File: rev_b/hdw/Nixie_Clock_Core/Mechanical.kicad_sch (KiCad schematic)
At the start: 40 parts

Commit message: lots of rev B control board schematic progress
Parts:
- renumbered H3101 to H?, H3104 to H?, H3106 to H?, H3102 to H?, H3103 to H?, H3107 to H?, H3105 to H?, H3108 to H?, MK3101 to MK?, MK3118 to MK?, MK3107 to MK?, MK3122 to MK?, MK3126 to MK?, MK3113 to MK?, MK3125 to MK?, MK3119 to MK?, MK3108 to MK?, MK3128 to MK?, MK3109 to MK?, MK3117 to MK?, MK3114 to MK?, MK3110 to MK?, MK3111 to MK?, MK3130 to MK?, MK3123 to MK?, MK3104 to MK?, MK3112 to MK?, MK3129 to MK?, MK3116 to MK?, MK3124 to MK?, MK3127 to MK?, MK3121 to MK?, MK3106 to MK?, MK3102 to MK?, MK3132 to MK?, MK3131 to MK?, MK3120 to MK?, MK3105 to MK?, MK3115 to MK?, MK3103 to MK?
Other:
- note added: "ENSURE STACK IS CORRECT HEIGHT"

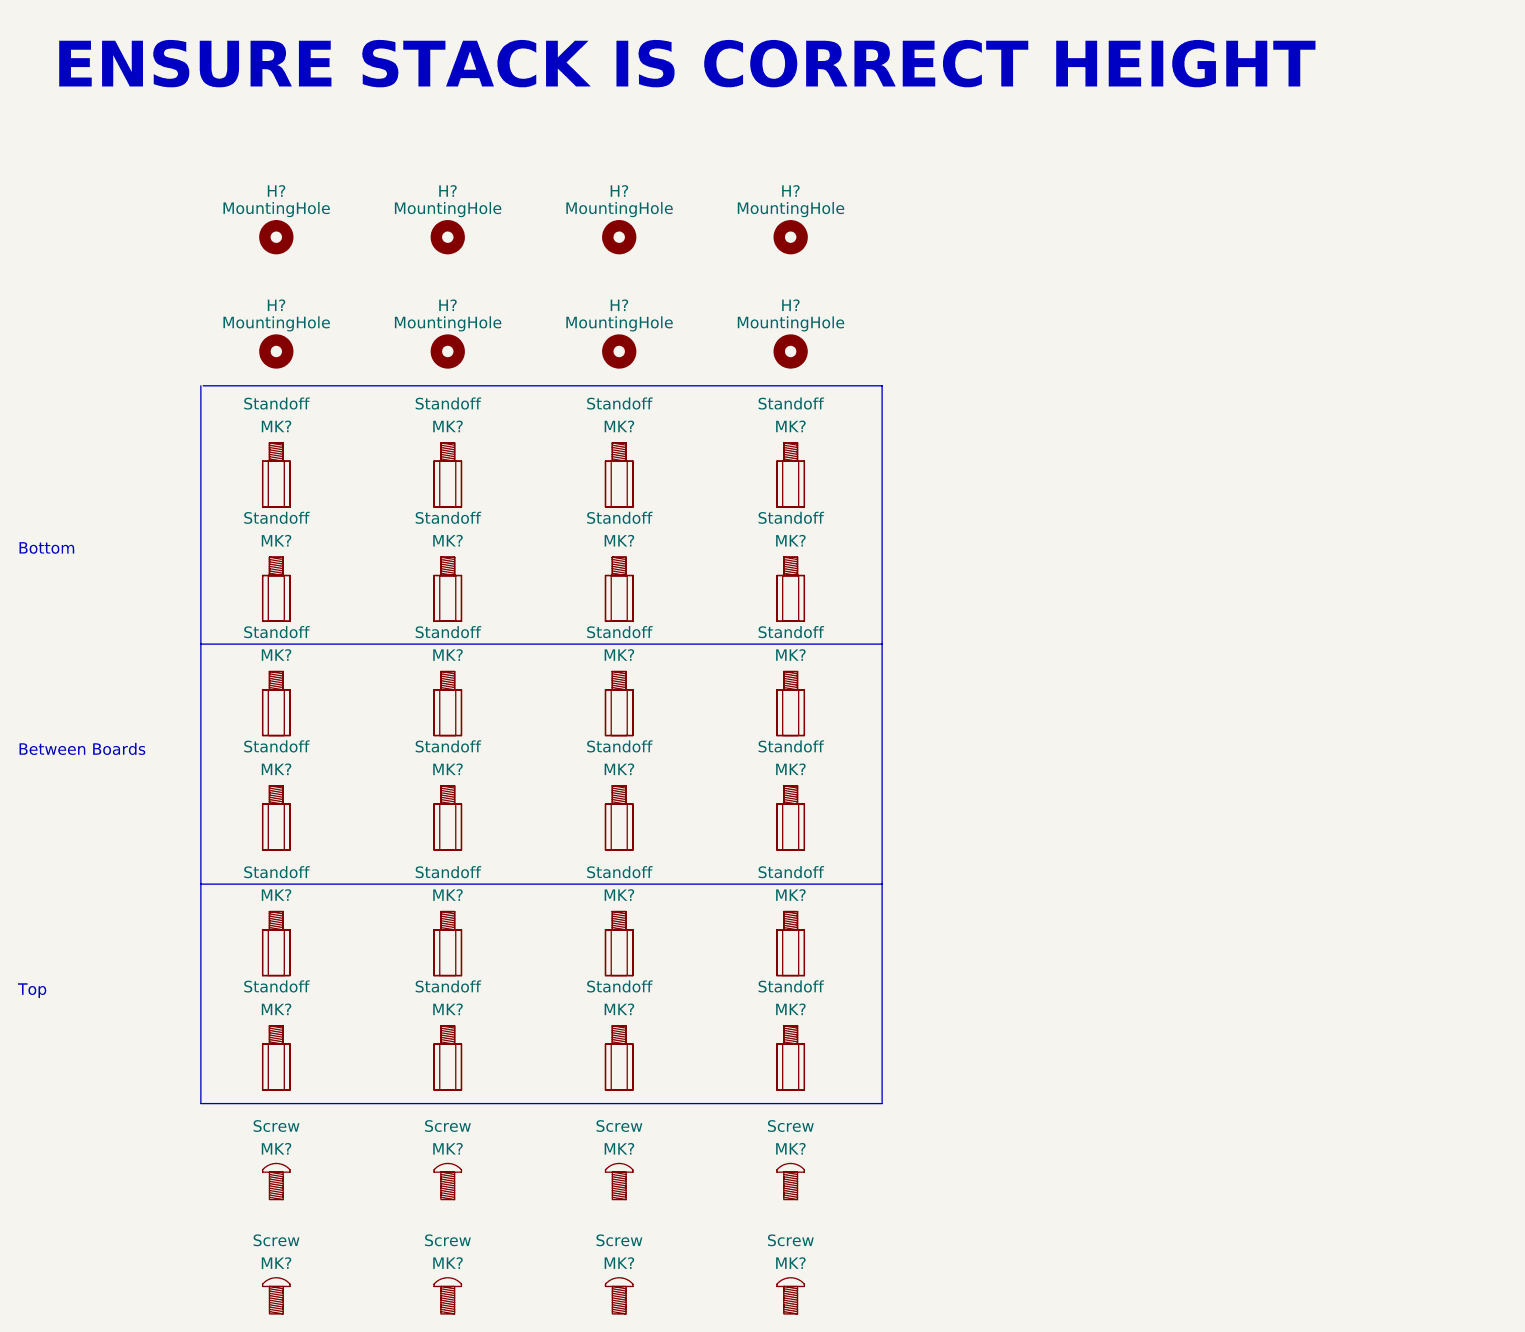
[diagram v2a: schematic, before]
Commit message: added BOM for IN12 carrier, finished routing, some schematic tweaks, adjusted design rules for ERC
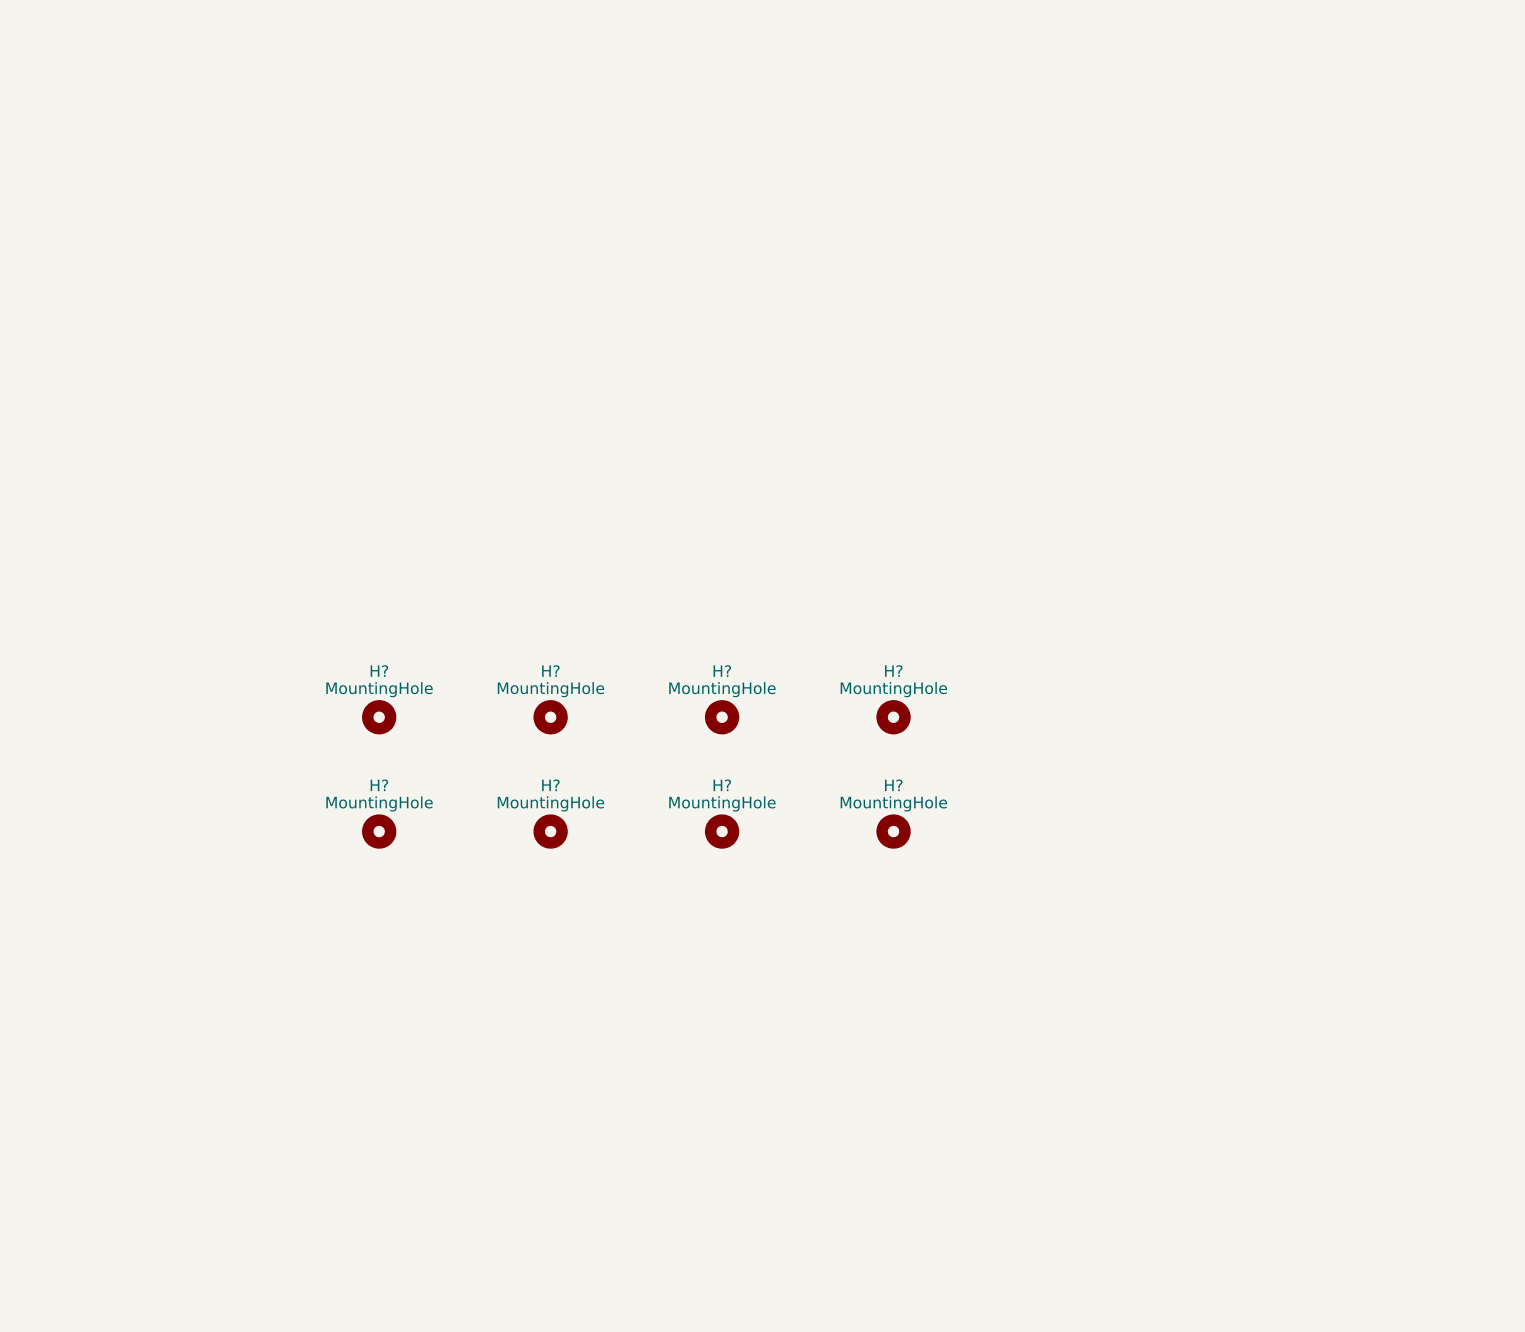
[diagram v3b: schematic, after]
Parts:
- removed MK? (x24): Standoff, symbol Custom_Library:Standoff
- removed MK? (x8): Screw, symbol Custom_Library:Screw
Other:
- note removed: "Between Boards"
- note removed: "Bottom"
- note removed: "ENSURE STACK IS CORRECT HEIGHT"
- note removed: "Top"
- moved on the sheet: H?

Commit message: added BOM
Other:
- title: (none) -> Nixie Clock Redux Core Board
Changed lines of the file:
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@@
   (paper "A")
   (title_block
-    (date "2023-05-12")
-    (rev "PRELIM")
+    (title "Nixie Clock Redux Core Board")
+    (date "2023-07-30")
+    (rev "B")
     (company "Drew Maatman")
   )
